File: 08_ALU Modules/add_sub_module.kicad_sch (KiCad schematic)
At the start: 15 parts, among them U1 74LS00, U2 74LS86, U3 74LS32, U4 74LS32, U5 74LS86, U6 74LS283, U7 74LS245, U8 74LS86, U9 74LS283

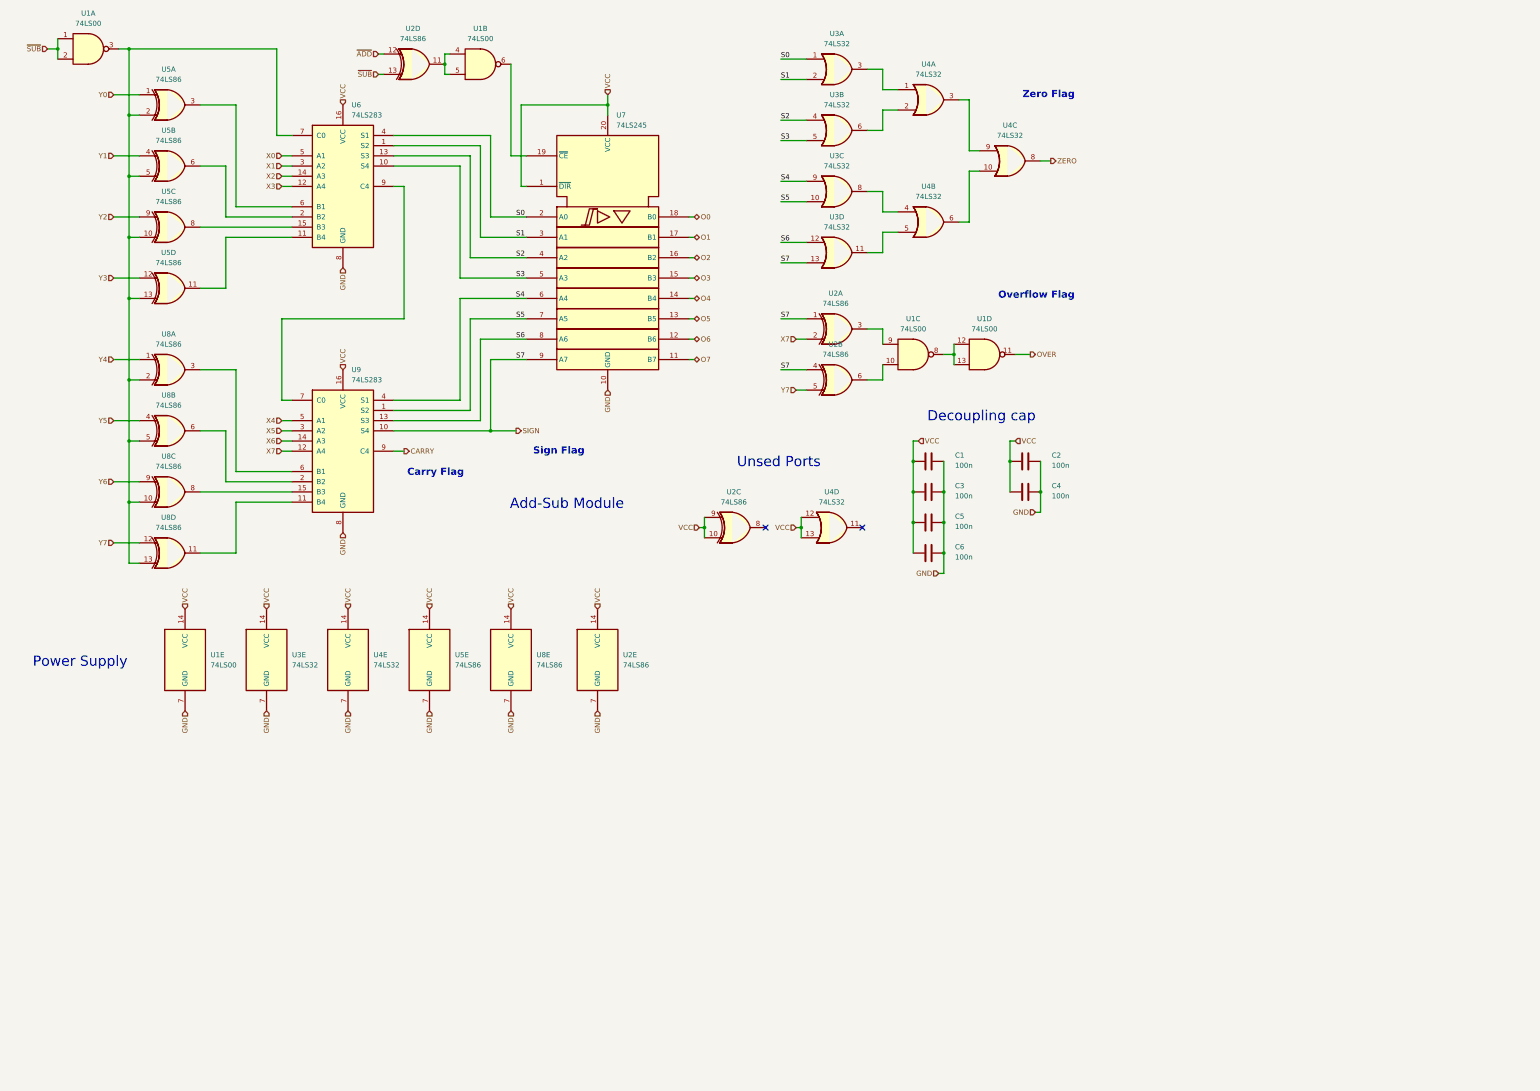
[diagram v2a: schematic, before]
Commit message: Update 10-01-2026 - Fixed bug on program counter - Fist ISA review, still in draft - Added missing mounting holes on memory modules
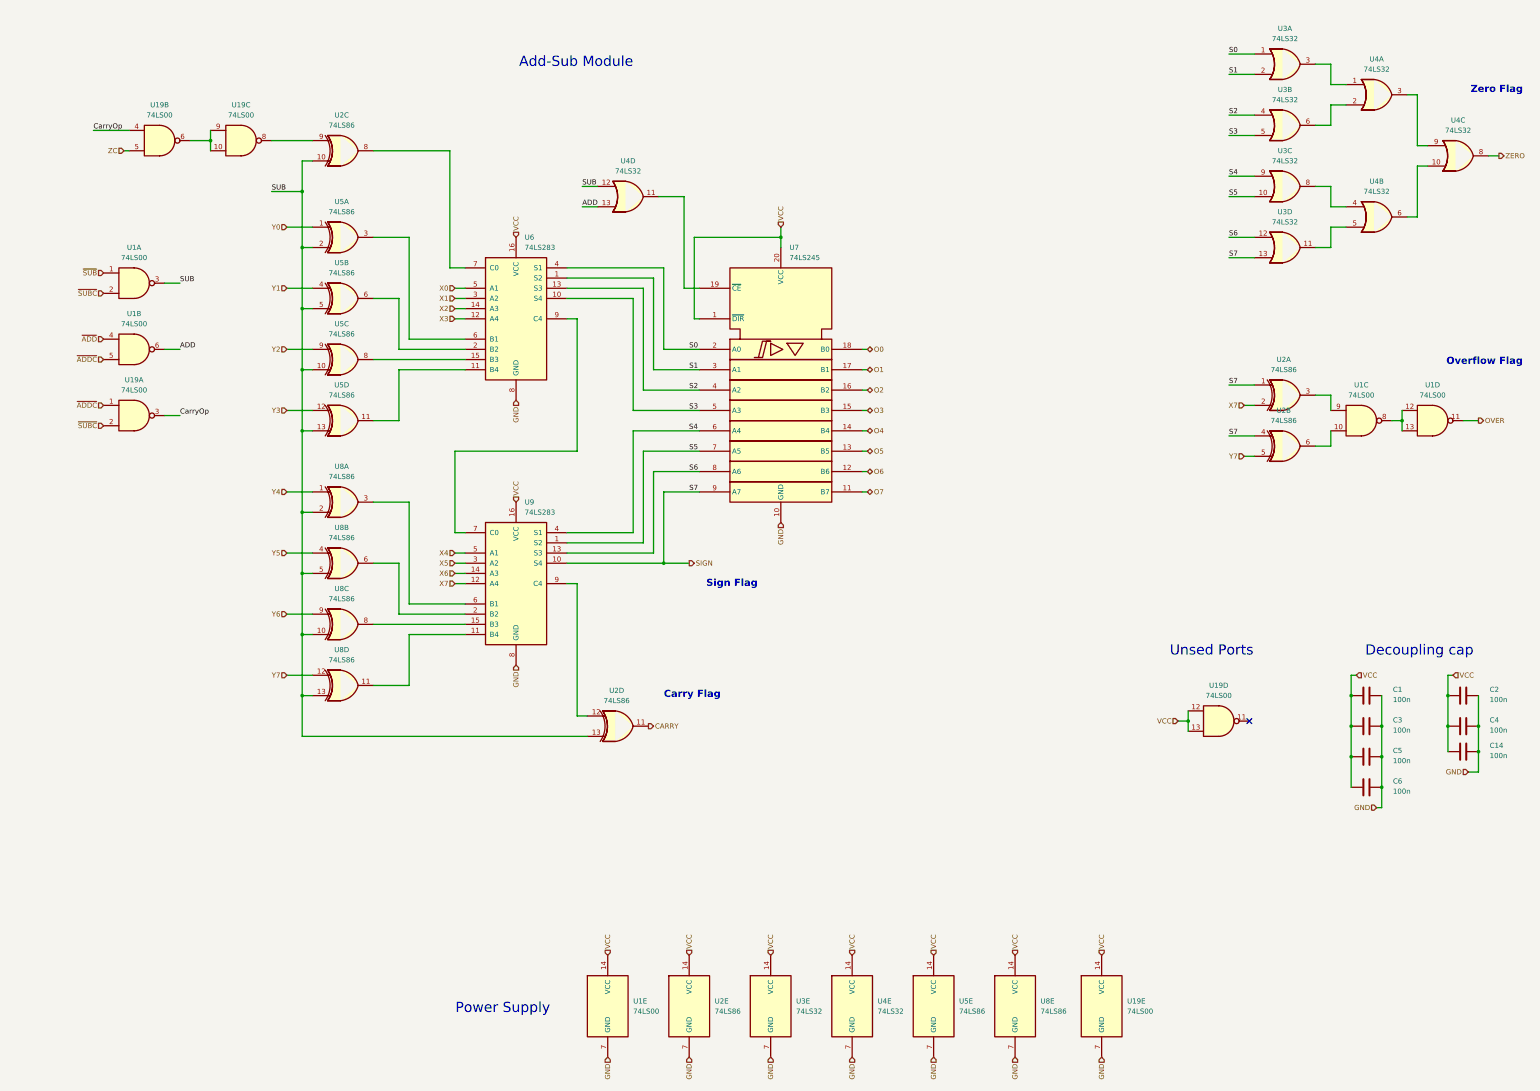
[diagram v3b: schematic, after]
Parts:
- added C14: 100n, Capacitor_THT:C_Disc_D3.0mm_W1.6mm_P2.50mm, symbol Device:C
- added U19: 74LS00, Package_DIP:DIP-14_W7.62mm, symbol 74xx:74LS00
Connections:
- net CARRY: now also U2.11; no longer U9.9 (C4)
- net GND: now also C14.2, U19.7 (GND)
- net VCC: now also C14.1, U19.12, U19.13, U19.14 (VCC); no longer U2.10, U2.9, U4.12, U4.13
- net ~{ADD}: now also U1.4; no longer U2.12
- net ~{SUB}: no longer U1.2, U2.13
- net SUB: now reaches U1.3, U5.10, U5.13, U5.2, U5.5, U8.10, U8.13, U8.2, U8.5
- net SUB: now also U2.10, U2.13, U4.12; no longer U6.7 (C0)
- net at U2.8: now also U6.7 (C0)
- net at U7.19 (~{CE}): now also U4.11; no longer U1.6
- new net: U19.8, U2.9
- new net: U2.12, U9.9 (C4)
- new net: U19.10, U19.6, U19.9
- new net ADD: U1.6, U4.13
- new net CarryOp: U19.3, U19.4
- new net ZC: U19.5
- new net ~{ADDC}: U1.5, U19.1
- new net ~{SUBC}: U1.2, U19.2
- no-connect marks 2 -> 1
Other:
- moved on the sheet: C1, C2, C3, C4, C5, C6, U1A, U1B, U1C, U1D, U1E, U2A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
